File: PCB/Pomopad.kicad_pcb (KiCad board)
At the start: 2 copper layers, 100 x 69.8 mm, 23 parts, among them J1 OLED, SW1 RotaryEncoder_Switch, SW2 SW_Push, SW3 SW_Push, SW4 SW_Push, SW5 SW_Push, SW6 SW_Push, SW7 SW_Push, U1 MOUDLE-SEEEDUINO-XIAO

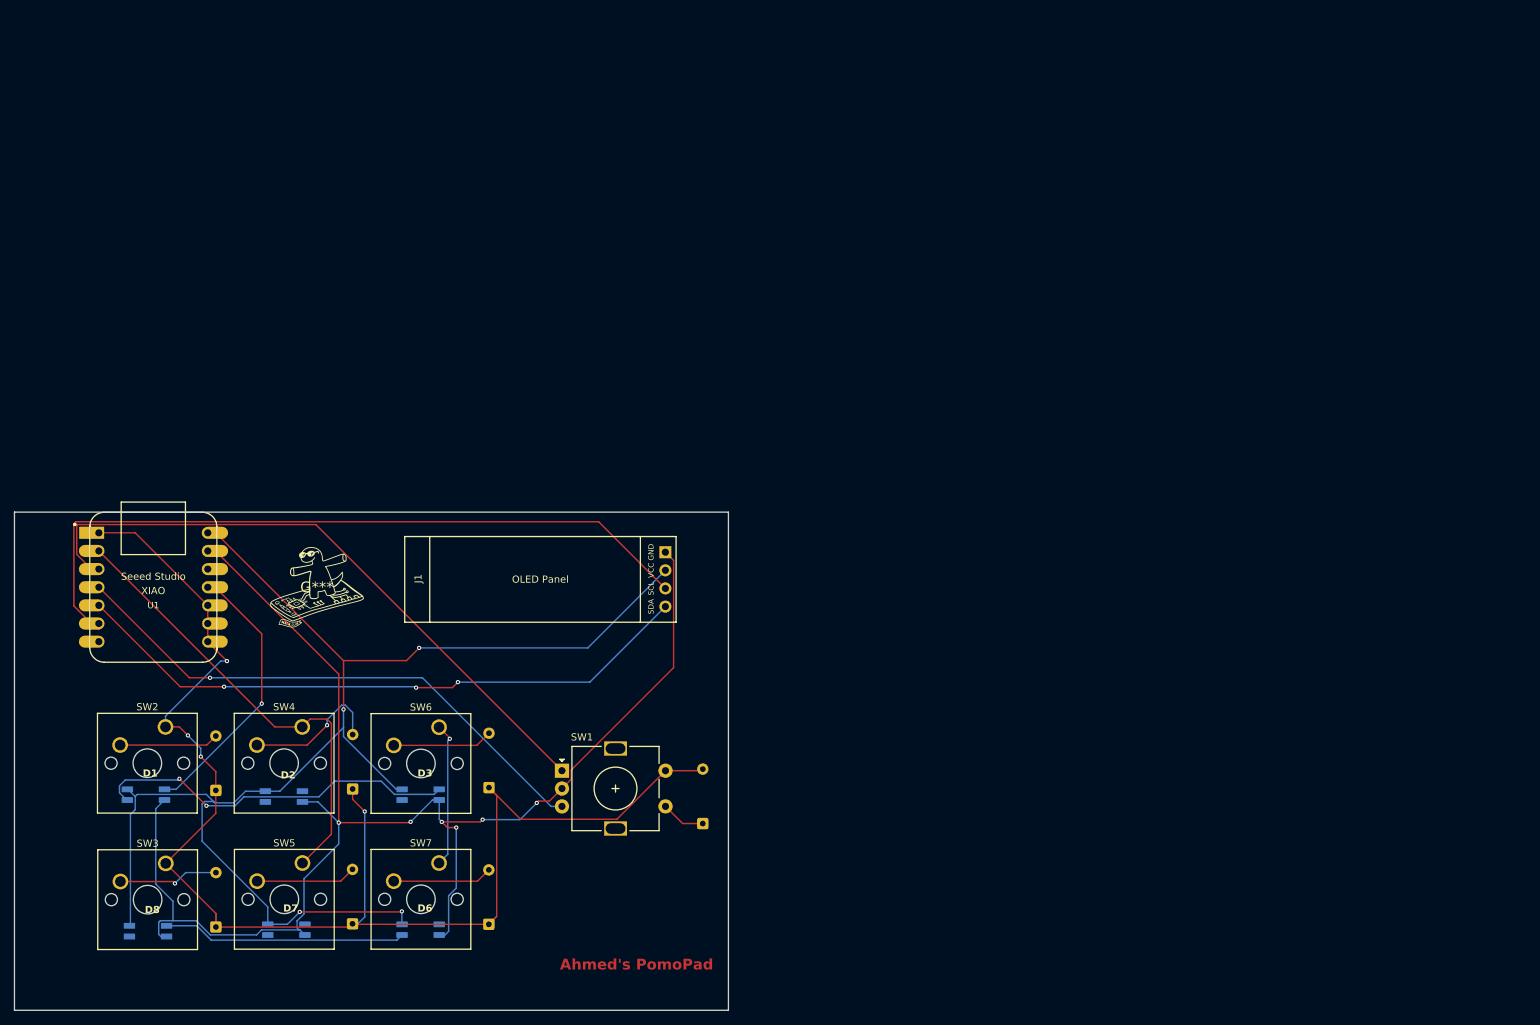
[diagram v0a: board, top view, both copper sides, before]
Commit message: Updated firmware: moved encoder push into matrix, set diode direction COL2ROW
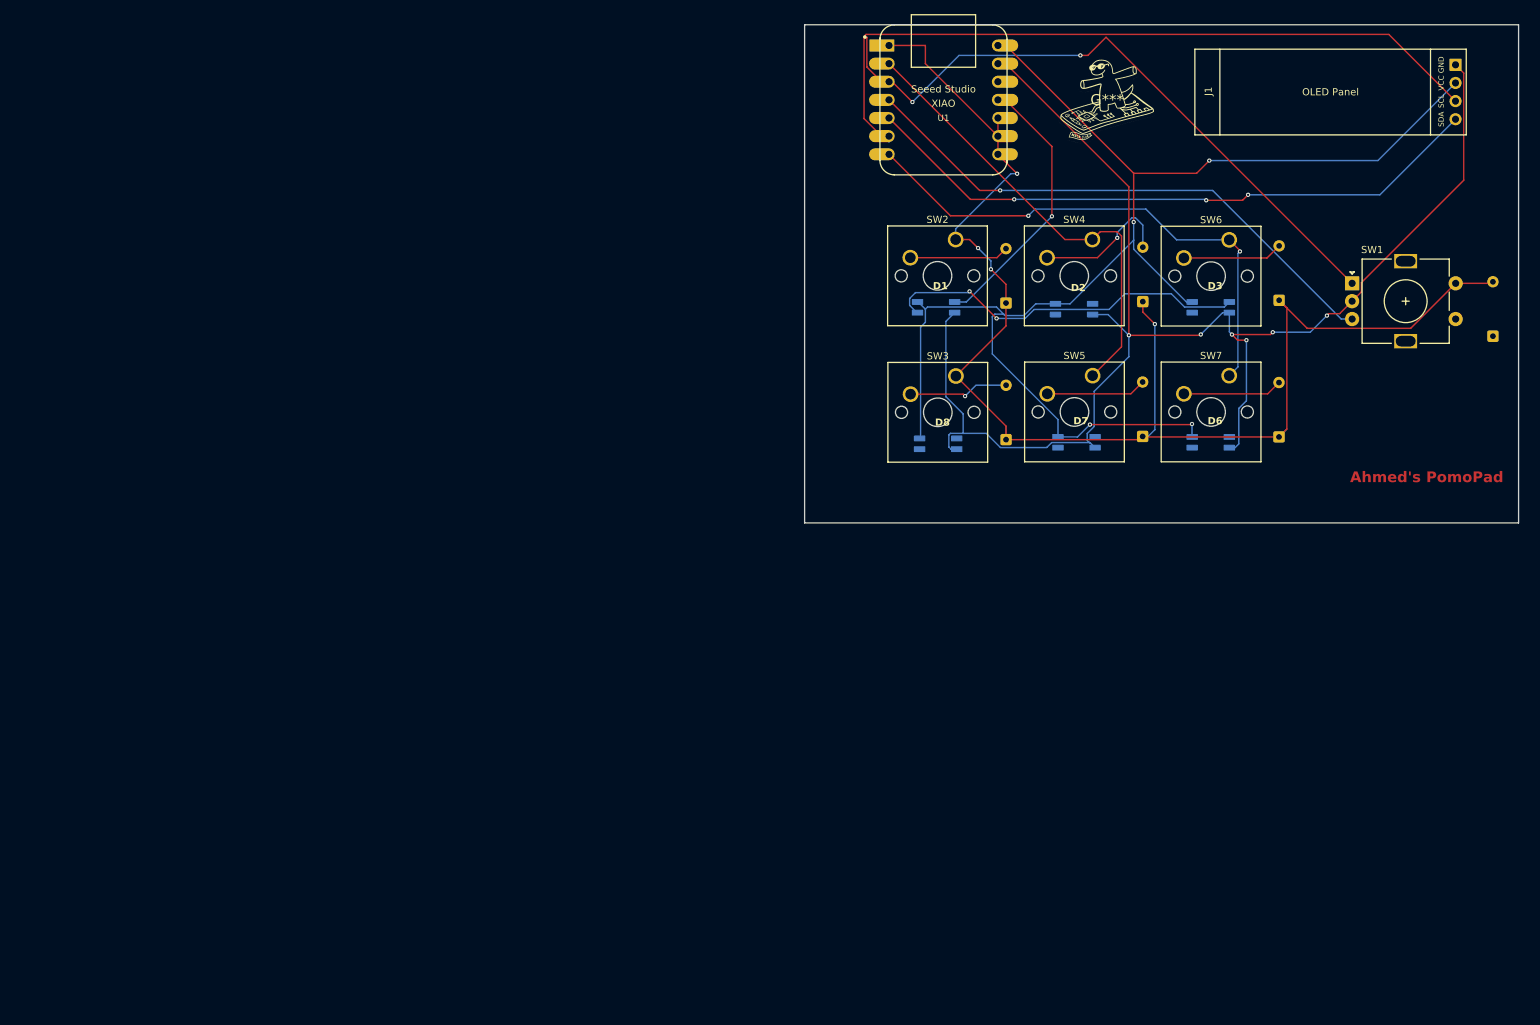
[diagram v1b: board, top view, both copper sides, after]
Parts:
- moved D13 130.0 mm to (177.9, 104.6)
- moved D17 130.0 mm to (216.1, 104.3)
- moved D6 130.0 mm to (206.6, 105.1)
- moved J1 130.0 mm to (204.4, 50.0)
- moved SW2 130.0 mm to (170.9, 76.6)
- moved SW6 130.0 mm to (209.2, 76.7)
- moved SW7 130.0 mm to (209.2, 95.7)
- moved D1 130.0 mm to (168.1, 86.2)
- moved D11 130.0 mm to (246.1, 90.1)
- moved D14 130.0 mm to (197.1, 85.3)
- moved D15 130.0 mm to (197.0, 104.2)
- moved D16 130.0 mm to (216.2, 85.1)
- moved D2 130.0 mm to (187.4, 86.5)
- moved D3 130.0 mm to (206.6, 86.2)
- moved D7 130.0 mm to (187.8, 105.1)
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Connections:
- D11 pad 1: Net-(D11-K) -> R2
- D6 pad 2: Net-(D6-DOUT) -> unconnected-(D6-DOUT-Pad2)
- SW1 pad S1: Net-(D11-K) -> Net-(D7-A)
- U1 pad 7: C3 -> C2
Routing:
- net C2: track 20.3 -> 73.6 mm, vias 1 -> 2
- net Net-(D6-DOUT): track 34.1 -> 0.00 mm
- net Net-(D11-K): track 6.21 -> 0.00 mm
- net C0: track 198.1 -> 202.3 mm
- net A: track 90.3 -> 92.2 mm, vias 0 -> 2
